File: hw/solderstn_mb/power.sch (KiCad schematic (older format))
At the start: 47 parts

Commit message: Summer vacation 2020 updates: * Front panel design rev 1 complete (incl Experimental outer board with optional linear touch sensors) * MB schematics AlmostDone(tm) - 'old' pinout supporting only one Rotary encoder * Lots of docs for new stuff
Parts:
- removed C?: UCL1V470MCL1GS, Capacitor_SMD:CP_Elec_6.3x5.8, symbol customlib_mj:UCL1V470MCL1GS
- removed D?: Red, symbol Device:LED_Small
- removed R?: 470R, symbol Device:R_Small
- added C302, C314, C315: 10u/16V, symbol Device:C_Small
- added C312, C313, C322: 10u, symbol Device:C_Small
- added C321: 100n, symbol Device:C_Small
- added D308: Green, symbol Device:LED_Small
- added D310: Red, symbol Device:LED_Small
- added FB301: 60R@100M, symbol Device:Ferrite_Bead_Small
- added Q301: Si4497DY, Package_SO:SO-8_3.9x4.9mm_P1.27mm, symbol customlib_mj:Si4497DY
- added Q302: DMG1012T, bobs:SOT-523, symbol customlib_mj:DMG1012T
- added R306: 1k, symbol Device:R_Small
- added R307: 10k, symbol Device:R_Small
- added R316: 100R, symbol Device:R_Small
- added R318: 470R, symbol Device:R_Small
- added U302: TLV1117LV30DCY, Package_TO_SOT_SMD:SOT-223-3_TabPin2, symbol customlib_mj:TLV1117LV30DCY
- gave numbers to parts that had none: 44
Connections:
- net +12V: now also C315.1, Q301.5 (D), Q301.6 (D), Q301.7 (D), Q301.8 (D)
- net GND: now also C302.2, C312.2, C313.2, C314.2, C315.2, C321.2, C322.2, D308.1 (K), Q302.2 (S), R307.2, U302.1 (GND)
- net VDD: now also R308.2, R318.1
- net VDDA: now also C322.1, FB301.1; no longer C320.1, U303.2 (VO)
- net VIN: now also C302.1, C314.1, Q301.1 (S), Q301.2 (S), Q301.3 (S), R306.1
- net VMAIN: now also C312.1, U302.3 (VI); no longer R308.2
- net ~VBUS2_FLG~ renamed ~VBUS2_FLGn~
- net ~VBUS2_FLGn~: now also D310.1 (K)
- new net: D310.2 (A), R318.2
- new net: C320.1, C321.1, FB301.2, U303.2 (VO)
- new net: Q301.4 (G), Q302.3 (D), R306.2
- new net: D308.2 (A), R316.2
- new net PWRDRV_ENABLE: Q302.1 (G), R307.1
- new net VDD_OLED: C313.1, R316.1, U302.2 (VO)
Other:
- note added: "3.0V analog\n(Vref, Vadc, Vop, etc)"
- note added: "3.0V digital\n(MCU etc)"
- note added: "High-side PFET master-switch\nfor the +12V PWM rail\n"
- note added: "ToDo: VIN connector? Screw terminals? Solderable \nthrough-holes? Cable-shoe spades?"
- note added: "VDD_OLED - Place LDO near \nthe frontpanel FFC connectors"
- note removed: "3.0V analogue"
- note removed: "3.0V digital"
- note removed: "TBD: hi/low..?"
- note removed: "ToDo: High-side P-FET\nmaster-switch for the\n+12V PWM rail. \nNeed rating Id >= 15A\n@ 12V Id, lowest RDS_on"
- note removed: "ToDo: VIN connector / solderable \nthrough-holes. Fuse?"
- moved on the sheet: C303, C304, C305, C306, C307, C308, C309, C310, C311, C316, C319, C320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

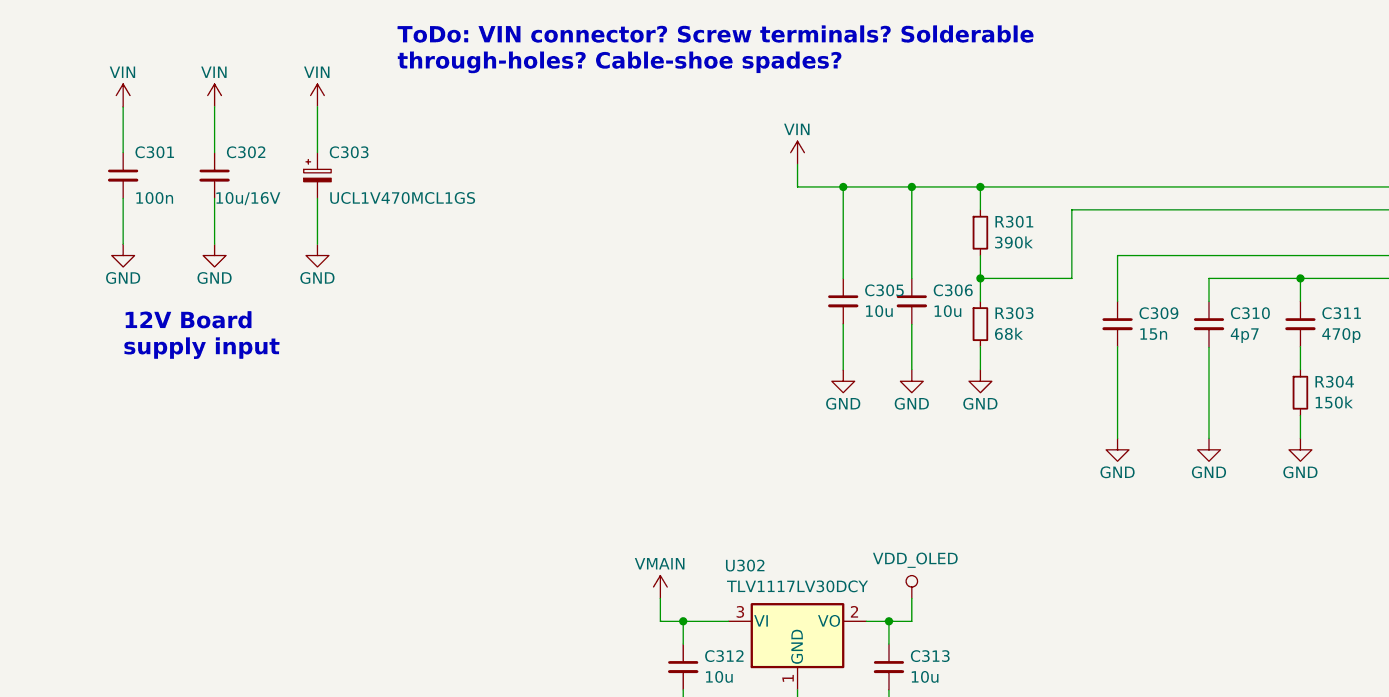
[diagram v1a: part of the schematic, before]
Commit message: Reverse-voltage protection PFET
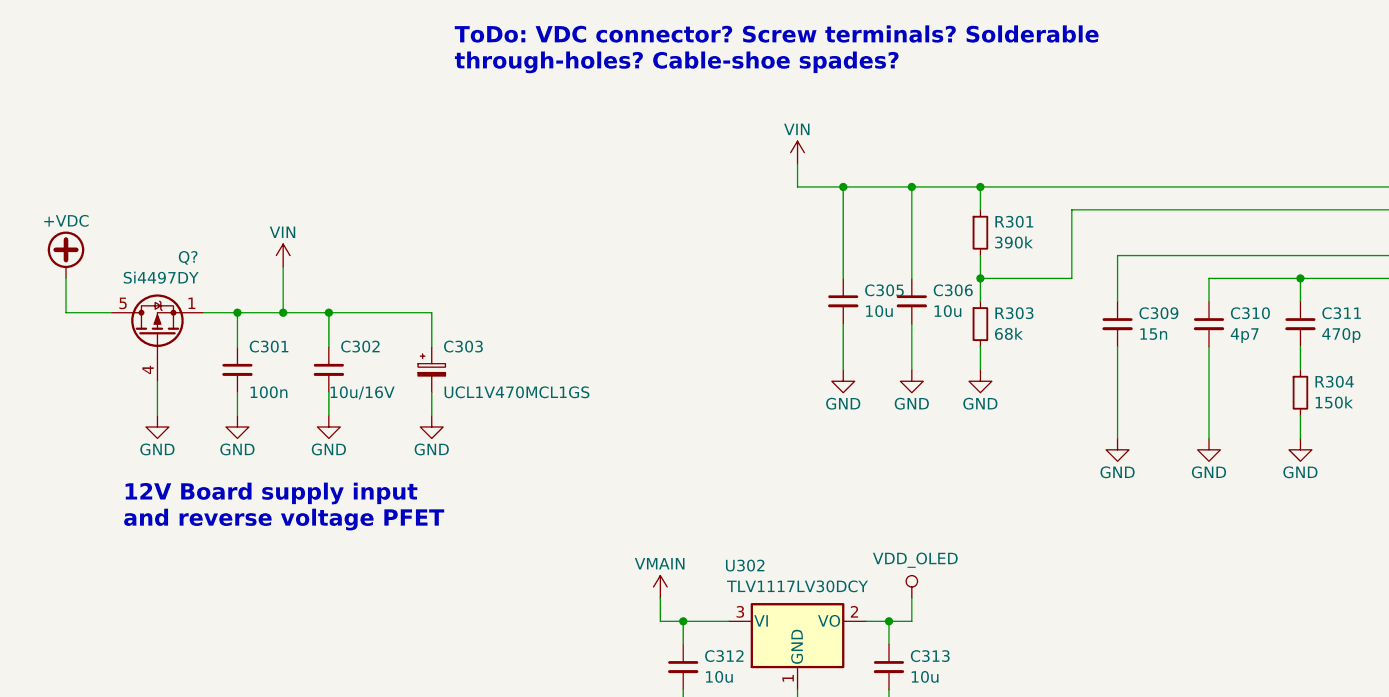
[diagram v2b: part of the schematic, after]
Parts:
- added Q?: Si4497DY, Package_SO:SO-8_3.9x4.9mm_P1.27mm, symbol customlib_mj:Si4497DY
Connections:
- net GND: now also Q?.4 (G)
- net VIN: now also Q?.1 (S), Q?.2 (S), Q?.3 (S)
- new net +VDC: Q?.5 (D), Q?.6 (D), Q?.7 (D), Q?.8 (D)
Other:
- note added: "12V Board supply input\nand reverse voltage PFET"
- note added: "ToDo: VDC connector? Screw terminals? Solderable \nthrough-holes? Cable-shoe spades?"
- note removed: "12V Board\nsupply input"
- note removed: "ToDo: VIN connector? Screw terminals? Solderable \nthrough-holes? Cable-shoe spades?"
- moved on the sheet: C301, C302, C303
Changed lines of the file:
@@
 L customlib_mj:VIN #PWR0301
 U 1 1 5F475C43
-P 900 1100
-F 0 "#PWR0301" H 900 950 50  0001 C CNN
-F 1 "VIN" H 900 1250 50  0000 C CNN
-F 2 "" H 900 1100 50  0001 C CNN
-F 3 "" H 900 1100 50  0001 C CNN
-	1    900  1100
+P 1600 1800
+F 0 "#PWR0301" H 1600 1650 50  0001 C CNN
+F 1 "VIN" H 1600 1950 50  0000 C CNN
+F 2 "" H 1600 1800 50  0001 C CNN
+F 3 "" H 1600 1800 50  0001 C CNN
+	1    1600 1800
 	1    0    0    -1
 $EndComp
@@
 L customlib_mj:UCL1V470MCL1GS C303
 U 1 1 5F47609B
-P 1750 1400
-F 0 "C303" H 1800 1500 50  0000 L CNN
-F 1 "UCL1V470MCL1GS" H 1800 1300 50  0000 L CNN
-F 2 "Capacitor_SMD:CP_Elec_6.3x5.8" H 1750 1400 50  0001 C CNN
-F 3 "https://www.mouser.se/datasheet/2/293/e-ucl-1513103.pdf" H 1750 1400 50  0001 C CNN
-	1    1750 1400
+P 2250 2250
+F 0 "C303" H 2300 2350 50  0000 L CNN
+F 1 "UCL1V470MCL1GS" H 2300 2150 50  0000 L CNN
+F 2 "Capacitor_SMD:CP_Elec_6.3x5.8" H 2250 2250 50  0001 C CNN
+F 3 "https://www.mouser.se/datasheet/2/293/e-ucl-1513103.pdf" H 2250 2250 50  0001 C CNN
+	1    2250 2250
 	1    0    0    -1
 $EndComp
@@
 L Device:C_Small C301
 U 1 1 5F476A64
-P 900 1400
-F 0 "C301" H 950 1500 50  0000 L CNN
-F 1 "100n" H 950 1300 50  0000 L CNN
-F 2 "" H 900 1400 50  0001 C CNN
-F 3 "~" H 900 1400 50  0001 C CNN
-	1    900  1400
+P 1400 2250
+F 0 "C301" H 1450 2350 50  0000 L CNN
+F 1 "100n" H 1450 2150 50  0000 L CNN
+F 2 "" H 1400 2250 50  0001 C CNN
+F 3 "~" H 1400 2250 50  0001 C CNN
+	1    1400 2250
 	1    0    0    -1
 $EndComp
@@
 L power:GND #PWR0308
 U 1 1 5F47714E
-P 1750 1700
-F 0 "#PWR0308" H 1750 1450 50  0001 C CNN
-F 1 "GND" H 1750 1550 50  0000 C CNN
-F 2 "" H 1750 1700 50  0001 C CNN
-F 3 "" H 1750 1700 50  0001 C CNN
-	1    1750 1700
-	1    0    0    -1
-$EndComp
-$Comp
-L customlib_mj:VIN #PWR0303
-U 1 1 5F4779C0
-P 1750 1100
-F 0 "#PWR0303" H 1750 950 50  0001 C CNN
-F 1 "VIN" H 1750 1250 50  0000 C CNN
-F 2 "" H 1750 1100 50  0001 C CNN
-F 3 "" H 1750 1100 50  0001 C CNN
-	1    1750 1100
+P 2250 2450
+F 0 "#PWR0308" H 2250 2200 50  0001 C CNN
+F 1 "GND" H 2250 2300 50  0000 C CNN
+F 2 "" H 2250 2450 50  0001 C CNN
+F 3 "" H 2250 2450 50  0001 C CNN
+	1    2250 2450
 	1    0    0    -1
 $EndComp
@@
 L power:GND #PWR0306
 U 1 1 5F477DAD
-P 900 1700
-F 0 "#PWR0306" H 900 1450 50  0001 C CNN
-F 1 "GND" H 900 1550 50  0000 C CNN
-F 2 "" H 900 1700 50  0001 C CNN
-F 3 "" H 900 1700 50  0001 C CNN
-	1    900  1700
-	1    0    0    -1
-$EndComp
-Wire Wire Line
-	900  1100 900  1300
-Wire Wire Line
-	1750 1100 1750 1300
-Wire Wire Line
-	1750 1500 1750 1700
-Wire Wire Line
-	900  1500 900  1700
-Text Notes 2100 950  0    71   ~ 14
-ToDo: VIN connector? Screw terminals? Solderable \nthrough-holes? Cable-shoe spades?
+P 1400 2450
+F 0 "#PWR0306" H 1400 2200 50  0001 C CNN
+F 1 "GND" H 1400 2300 50  0000 C CNN
+F 2 "" H 1400 2450 50  0001 C CNN
+F 3 "" H 1400 2450 50  0001 C CNN
+	1    1400 2450
+	1    0    0    -1
+$EndComp
+Wire Wire Line
+	2250 2350 2250 2450
+Wire Wire Line
+	1400 2350 1400 2450
+Text Notes 2350 950  0    71   ~ 14
+ToDo: VDC connector? Screw terminals? Solderable \nthrough-holes? Cable-shoe spades?
 $Comp
 L power:GND #PWR0333
@@
 Text Notes 1800 7300 0    71   ~ 14
 Power LED indicators
-Text Notes 900  2200 0    71   ~ 14
-12V Board\nsupply input
+Text Notes 900  2950 0    71   ~ 14
+12V Board supply input\nand reverse voltage PFET
 Wire Wire Line
 	8350 4500 8900 4500
@@
 $EndComp
 $Comp
-L customlib_mj:VIN #PWR0302
-U 1 1 5F4B4858
-P 1300 1100
-F 0 "#PWR0302" H 1300 950 50  0001 C CNN
-F 1 "VIN" H 1300 1250 50  0000 C CNN
-F 2 "" H 1300 1100 50  0001 C CNN
-F 3 "" H 1300 1100 50  0001 C CNN
-	1    1300 1100
-	1    0    0    -1
-$EndComp
-$Comp
 L Device:C_Small C302
 U 1 1 5F4B4862
-P 1300 1400
-F 0 "C302" H 1350 1500 50  0000 L CNN
-F 1 "10u/16V" H 1300 1300 50  0000 L CNN
-F 2 "" H 1300 1400 50  0001 C CNN
-F 3 "~" H 1300 1400 50  0001 C CNN
-	1    1300 1400
+P 1800 2250
+F 0 "C302" H 1850 2350 50  0000 L CNN
+F 1 "10u/16V" H 1800 2150 50  0000 L CNN
+F 2 "" H 1800 2250 50  0001 C CNN
+F 3 "~" H 1800 2250 50  0001 C CNN
+	1    1800 2250
 	1    0    0    -1
 $EndComp
@@
 L power:GND #PWR0307
 U 1 1 5F4B486C
-P 1300 1700
-F 0 "#PWR0307" H 1300 1450 50  0001 C CNN
-F 1 "GND" H 1300 1550 50  0000 C CNN
-F 2 "" H 1300 1700 50  0001 C CNN
-F 3 "" H 1300 1700 50  0001 C CNN
-	1    1300 1700
-	1    0    0    -1
-$EndComp
-Wire Wire Line
-	1300 1100 1300 1300
-Wire Wire Line
-	1300 1500 1300 1700
+P 1800 2450
+F 0 "#PWR0307" H 1800 2200 50  0001 C CNN
+F 1 "GND" H 1800 2300 50  0000 C CNN
+F 2 "" H 1800 2450 50  0001 C CNN
+F 3 "" H 1800 2450 50  0001 C CNN
+	1    1800 2450
+	1    0    0    -1
+$EndComp
+Wire Wire Line
+	1800 2350 1800 2450
 $Comp
 L Device:C_Small C314
@@
 Text Notes 3550 5550 0    71   ~ 14
 3.0V digital\n(MCU etc)
+$Comp
+L customlib_mj:Si4497DY Q?
+U 1 1 5F6AC6C1
+P 1050 2100
+F 0 "Q?" V 1392 1920 50  0000 L CNN
+F 1 "Si4497DY" V 1301 1920 50  0000 L CNN
+F 2 "Package_SO:SO-8_3.9x4.9mm_P1.27mm" H 1250 2025 50  0001 L CIN
+F 3 "https://www.vishay.com/docs/65748/si4497dy.pdf" H 1050 2100 50  0001 L CNN
+	1    1050 2100
+	0    -1   -1   0
+$EndComp
+$Comp
+L power:+VDC #PWR?
+U 1 1 5F6AF81A
+P 650 1850
+F 0 "#PWR?" H 650 1750 50  0001 C CNN
+F 1 "+VDC" H 650 2100 50  0000 C CNN
+F 2 "" H 650 1850 50  0001 C CNN
+F 3 "" H 650 1850 50  0001 C CNN
+	1    650  1850
+	1    0    0    -1
+$EndComp
+Wire Wire Line
+	1250 2000 1400 2000
+Wire Wire Line
+	850  2000 650  2000
+Wire Wire Line
+	650  2000 650  1850
+$Comp
+L power:GND #PWR?
+U 1 1 5F6C66F3
+P 1050 2450
+F 0 "#PWR?" H 1050 2200 50  0001 C CNN
+F 1 "GND" H 1050 2300 50  0000 C CNN
+F 2 "" H 1050 2450 50  0001 C CNN
+F 3 "" H 1050 2450 50  0001 C CNN
+	1    1050 2450
+	1    0    0    -1
+$EndComp
+Wire Wire Line
+	1050 2450 1050 2300
+Wire Wire Line
+	2250 2000 2250 2150
+Wire Wire Line
+	1800 2000 1800 2150
+Connection ~ 1800 2000
+Wire Wire Line
+	1800 2000 2250 2000
+Wire Wire Line
+	1600 2000 1600 1800
+Connection ~ 1600 2000
+Wire Wire Line
+	1600 2000 1800 2000
+Wire Wire Line
+	1400 2000 1400 2150
+Connection ~ 1400 2000
+Wire Wire Line
+	1400 2000 1600 2000
 $EndSCHEMATC

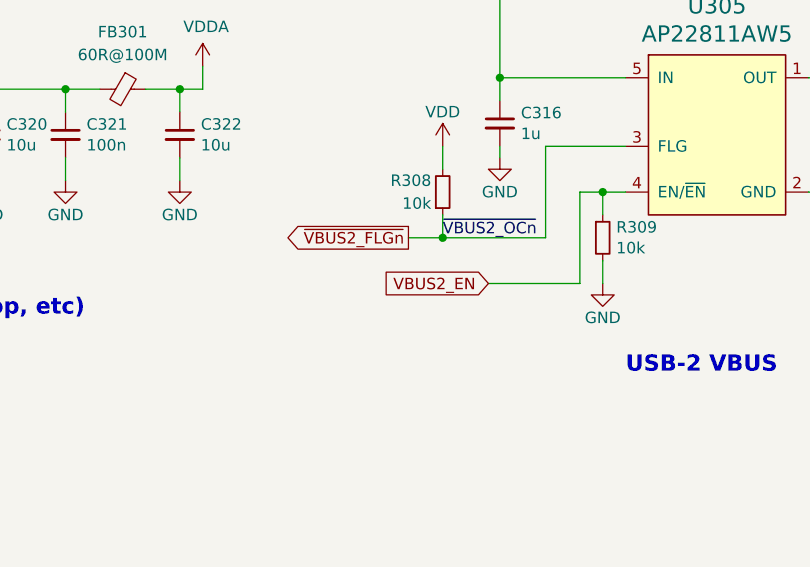
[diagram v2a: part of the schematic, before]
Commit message: Update pinout to "alternative", shuffling stuff around to optionally support a 2nd rotary on front-panel (corresponding Front-panel side not yet updated)
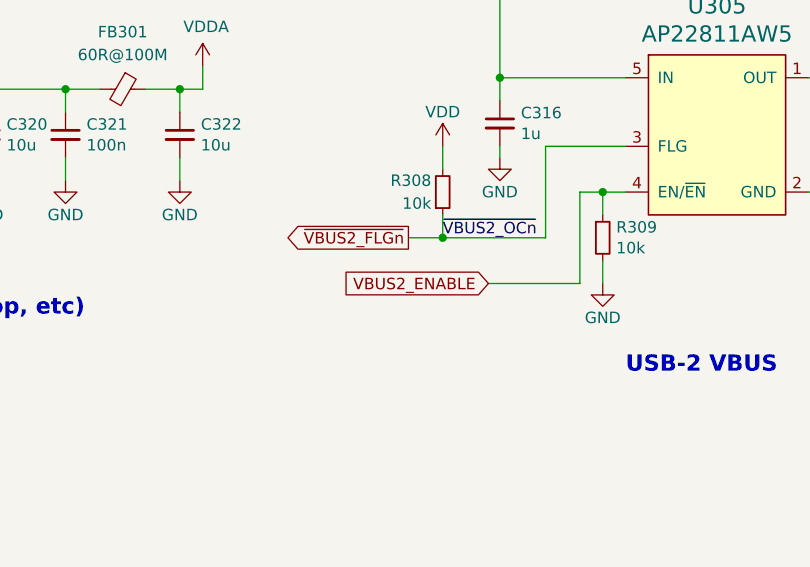
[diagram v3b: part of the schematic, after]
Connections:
- net VBUS2_EN renamed VBUS2_ENABLE
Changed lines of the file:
@@
 ~VBUS2_FLGn~
 Text GLabel 8300 5400 0    50   Input ~ 0
-VBUS2_EN
+VBUS2_ENABLE
 Wire Wire Line
 	1550 4800 1500 4800

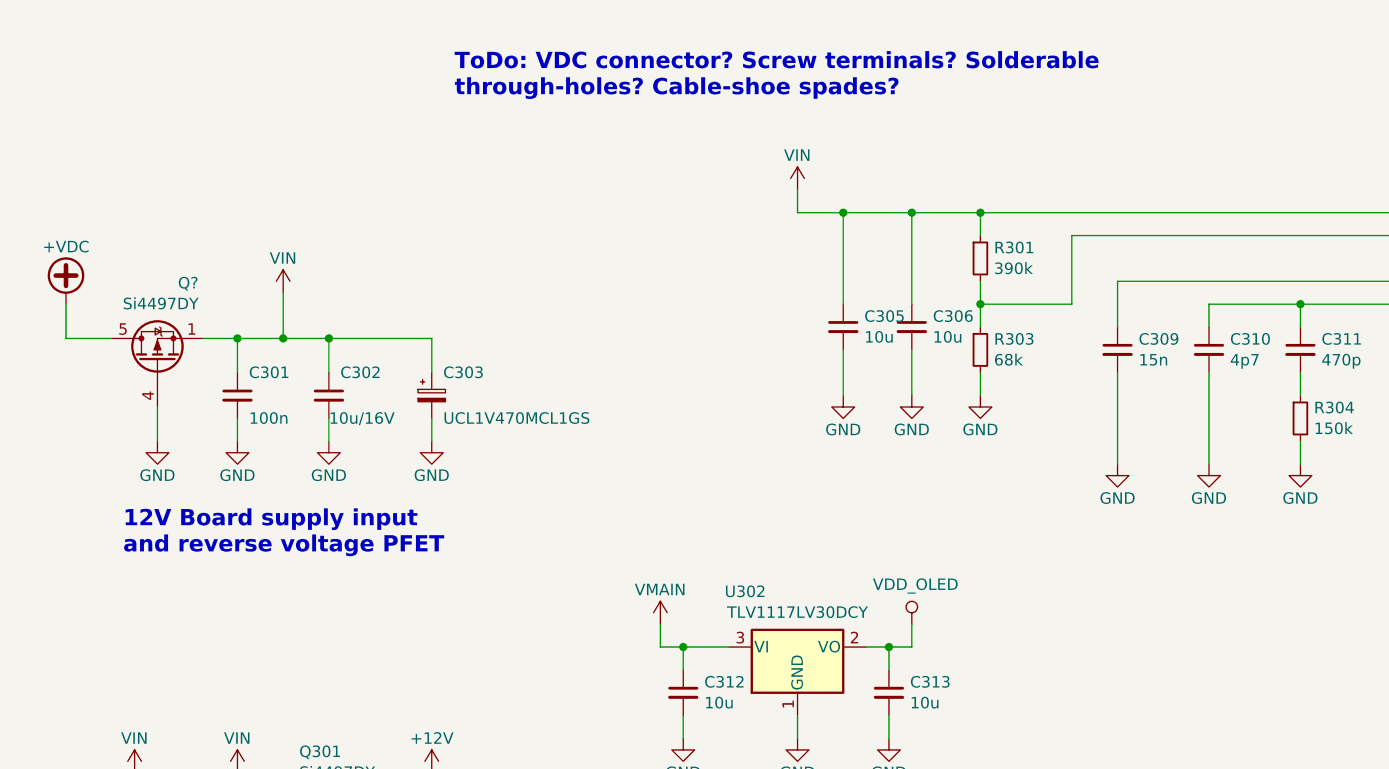
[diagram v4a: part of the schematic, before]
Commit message: * Added Molex connectors (PwrLED-conn, DC-in, FM-ant.) * Renamed Si4735 doc dir
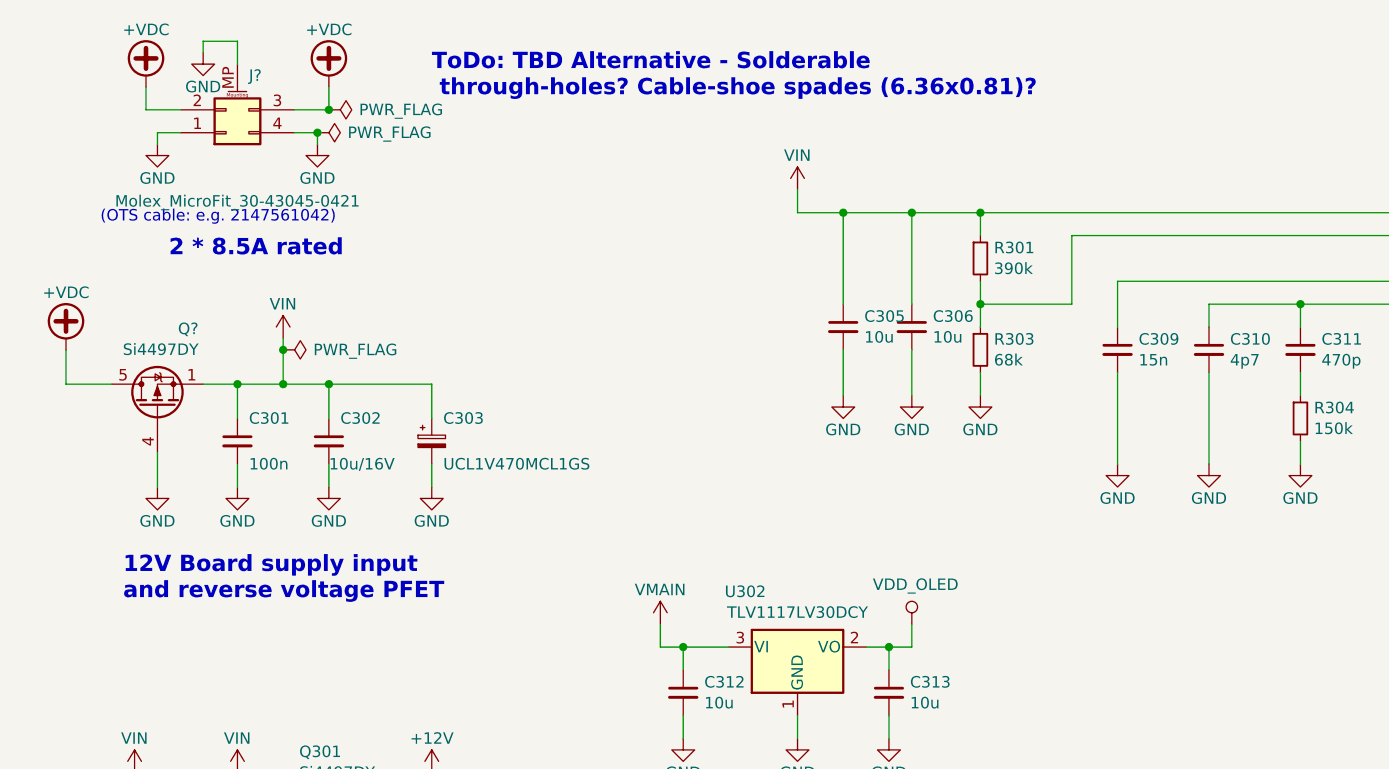
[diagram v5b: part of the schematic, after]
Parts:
- added J?: Molex_MicroFit_30-43045-0421, Connector_Molex:Molex_Micro-Fit_3.0_43045-0421_2x02-1MP_P3.00mm_Horizontal, symbol Connector_Generic_MountingPin:Conn_02x02_Counter_Clockwise_MountingPin
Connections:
- net +VDC: now also J?.2 (Pin_2), J?.3 (Pin_3)
- net GND: now also J?.1 (Pin_1), J?.4 (Pin_4), J?.MP (MountPin)
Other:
- note added: "(OTS cable: e.g. 2147561042)"
- note added: "2 * 8.5A rated"
- note added: "ToDo: TBD Alternative - Solderable\n through-holes? Cable-shoe spades (6.36x0.81)?"
- note removed: "ToDo: VDC connector? Screw terminals? Solderable \nthrough-holes? Cable-shoe spades?"
- moved on the sheet: C301, C302, C303, Q?
